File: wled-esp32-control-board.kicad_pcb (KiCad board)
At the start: 4 copper layers, 64.9 x 39.5 mm, 53 parts, among them J101 Conn_01x03, J102 Conn_01x03, J103 Conn_01x03, J104 Conn_01x03, J105 Conn_02x03_Odd_Even, J201 USB_C_Receptacle_USB2.0, Q401 MMDT3904, SW101 SW_SPDT, SW103 SW_Push, SW105 SW_Push, U101 74AHCT1G125, U102 74AHCT1G125, U103 ESP32-WROOM-32, U104 74AHCT1G125, U105 74AHCT1G125, U106 TSOP382xx, U301 XC6220B331MR-G, U401 CP2102-GMR

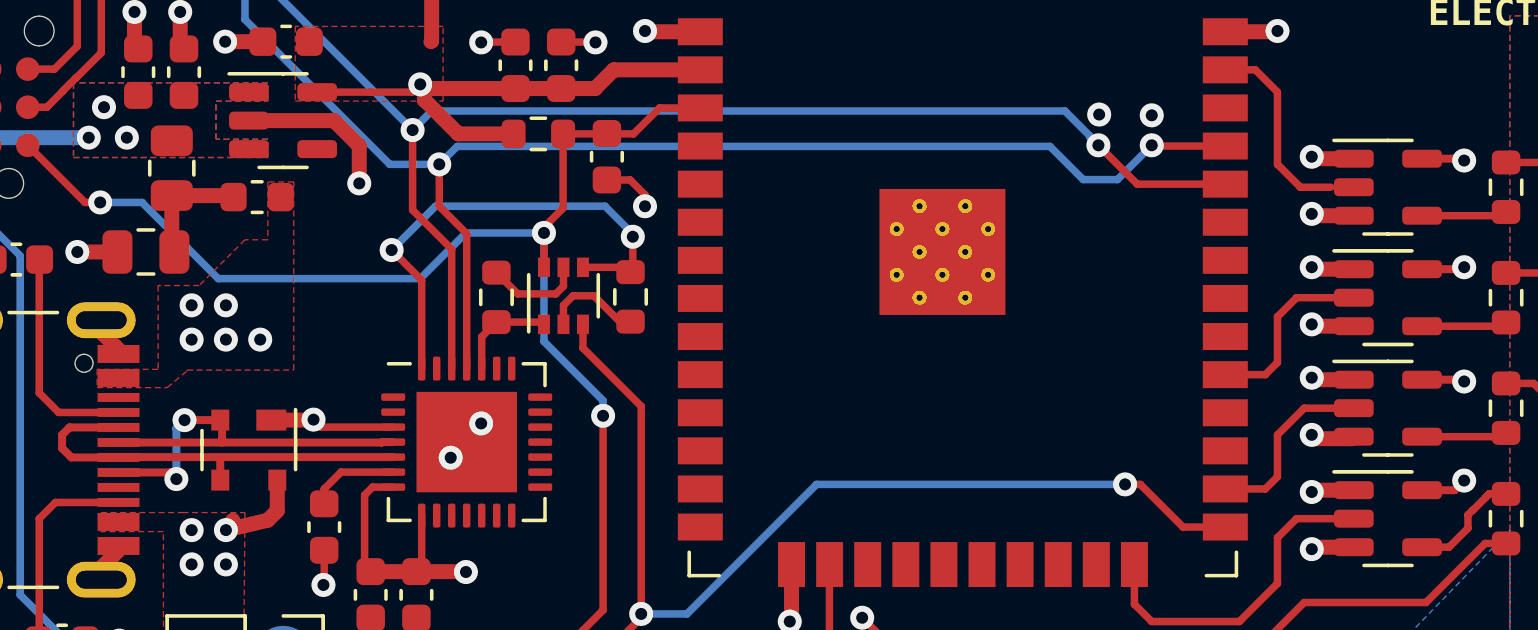
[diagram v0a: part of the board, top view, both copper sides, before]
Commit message: fix short traces
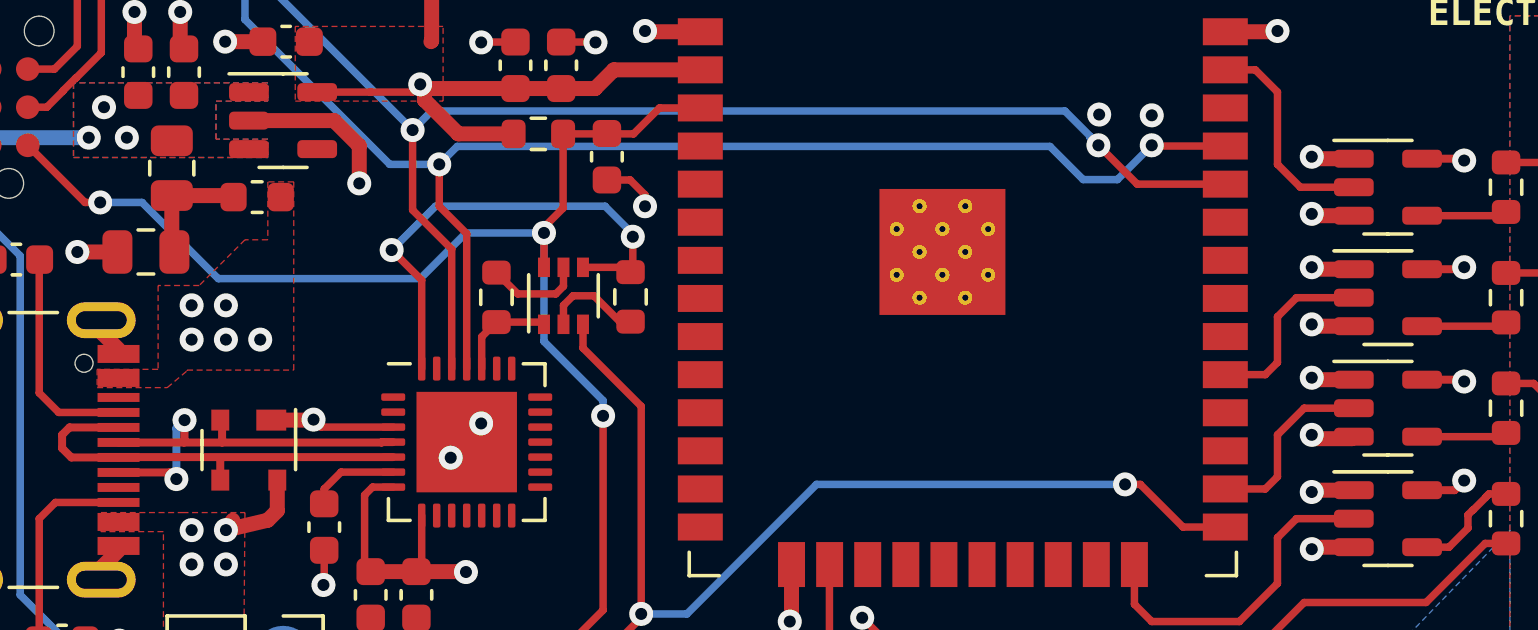
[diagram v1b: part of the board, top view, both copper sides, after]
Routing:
- net /LED0: track 6.55 -> 7.32 mm
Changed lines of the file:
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@@
   (segment (start 111.8616 91.9734) (end 112.424 91.411) (width 0.25) (layer "F.Cu") (net 7))
   (segment (start 111.8616 92.4684) (end 111.8616 91.9734) (width 0.25) (layer "F.Cu") (net 7))
+  (segment (start 107.205174 90.408626) (end 107.188 90.4258) (width 0.2672) (layer "F.Cu") (net 8))
   (segment (start 105.0088 90.4258) (end 105.006 90.423) (width 0.2672) (layer "F.Cu") (net 8))
   (segment (start 106.934 91.6441) (end 106.7129 91.423) (width 0.2672) (layer "F.Cu") (net 8))
@@
   (segment (start 108.458 89.739) (end 108.397 89.678) (width 0.2672) (layer "F.Cu") (net 8))
   (segment (start 113.789999 90.411) (end 113.775199 90.4258) (width 0.2672) (layer "F.Cu") (net 8))
-  (segment (start 107.205174 89.679174) (end 107.206348 89.678) (width 0.2672) (layer "F.Cu") (net 8))
-  (segment (start 107.206348 89.678) (end 108.397 89.678) (width 0.2672) (layer "F.Cu") (net 8))
+  (segment (start 107.205174 89.679174) (end 107.205174 90.408626) (width 0.2672) (layer "F.Cu") (net 8))
   (segment (start 114.1614 90.411) (end 113.789999 90.411) (width 0.2672) (layer "F.Cu") (net 8))
   (segment (start 113.775199 90.4258) (end 105.0088 90.4258) (width 0.2672) (layer "F.Cu") (net 8))
@@
   (segment (start 149.3545 93.914) (end 148.4575 93.914) (width 0.25) (layer "F.Cu") (net 32))
   (segment (start 150.585 92.239) (end 150.585 92.248305) (width 0.25) (layer "F.Cu") (net 32))
+  (segment (start 141.8985 78.003) (end 142.8985 78.003) (width 0.25) (layer "F.Cu") (net 33))
+  (segment (start 142.8985 78.003) (end 143.637 78.7415) (width 0.25) (layer "F.Cu") (net 33))
+  (segment (start 144.399 81.915) (end 146.1825 81.915) (width 0.25) (layer "F.Cu") (net 33))
   (segment (start 143.637 81.153) (end 144.399 81.915) (width 0.25) (layer "F.Cu") (net 33))
-  (segment (start 141.8985 78.003) (end 142.8985 78.003) (width 0.25) (layer "F.Cu") (net 33))
   (segment (start 143.637 78.7415) (end 143.637 81.153) (width 0.25) (layer "F.Cu") (net 33))
-  (segment (start 144.399 81.915) (end 145.415 81.915) (width 0.25) (layer "F.Cu") (net 33))
-  (segment (start 142.8985 78.003) (end 143.637 78.7415) (width 0.25) (layer "F.Cu") (net 33))
   (segment (start 143.637 86.233) (end 144.272 85.598) (width 0.25) (layer "F.Cu") (net 34))
   (segment (start 143.637 87.757) (end 143.637 86.233) (width 0.25) (layer "F.Cu") (net 34))

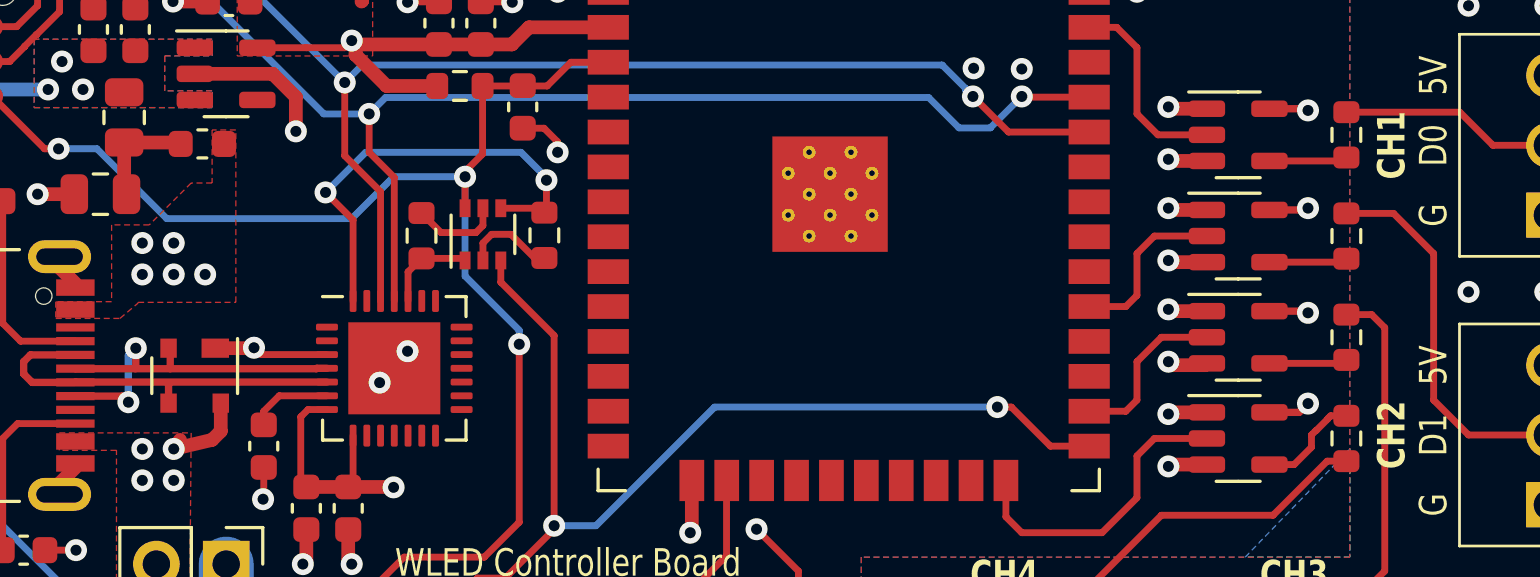
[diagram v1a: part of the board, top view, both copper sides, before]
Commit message: add teardrops
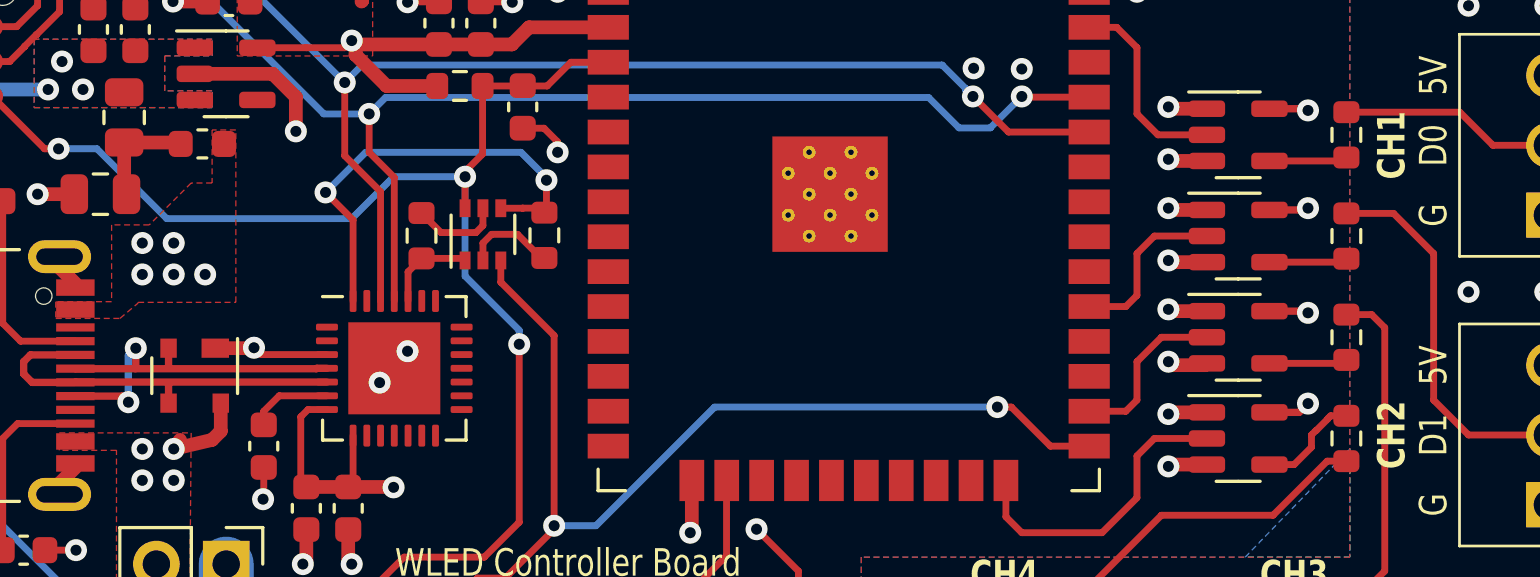
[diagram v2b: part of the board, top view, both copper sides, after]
